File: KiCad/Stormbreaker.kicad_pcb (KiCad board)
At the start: 4 copper layers, 50.2 x 21 mm, 45 parts, among them J1 Micro_SD_Card_Det2, J2 USB_C_Receptacle_USB2.0_14P, J3 Conn_01x03, J4 FAN, Q1 PMOS, Q2 NMOS, SW1 SW_Push, U1 BQ25895RTW, U3 ATtiny1616-M

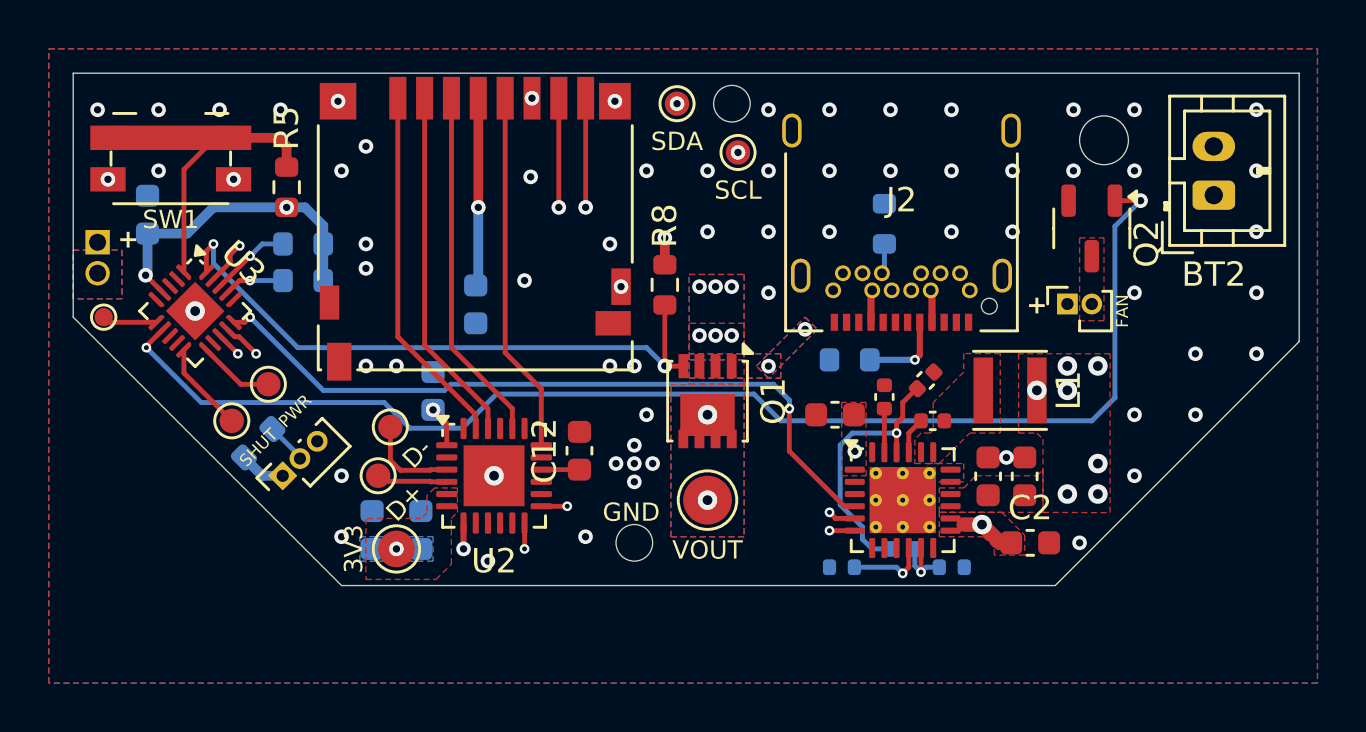
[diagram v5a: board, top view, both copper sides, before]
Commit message: Power and ground zones, gnd stitching
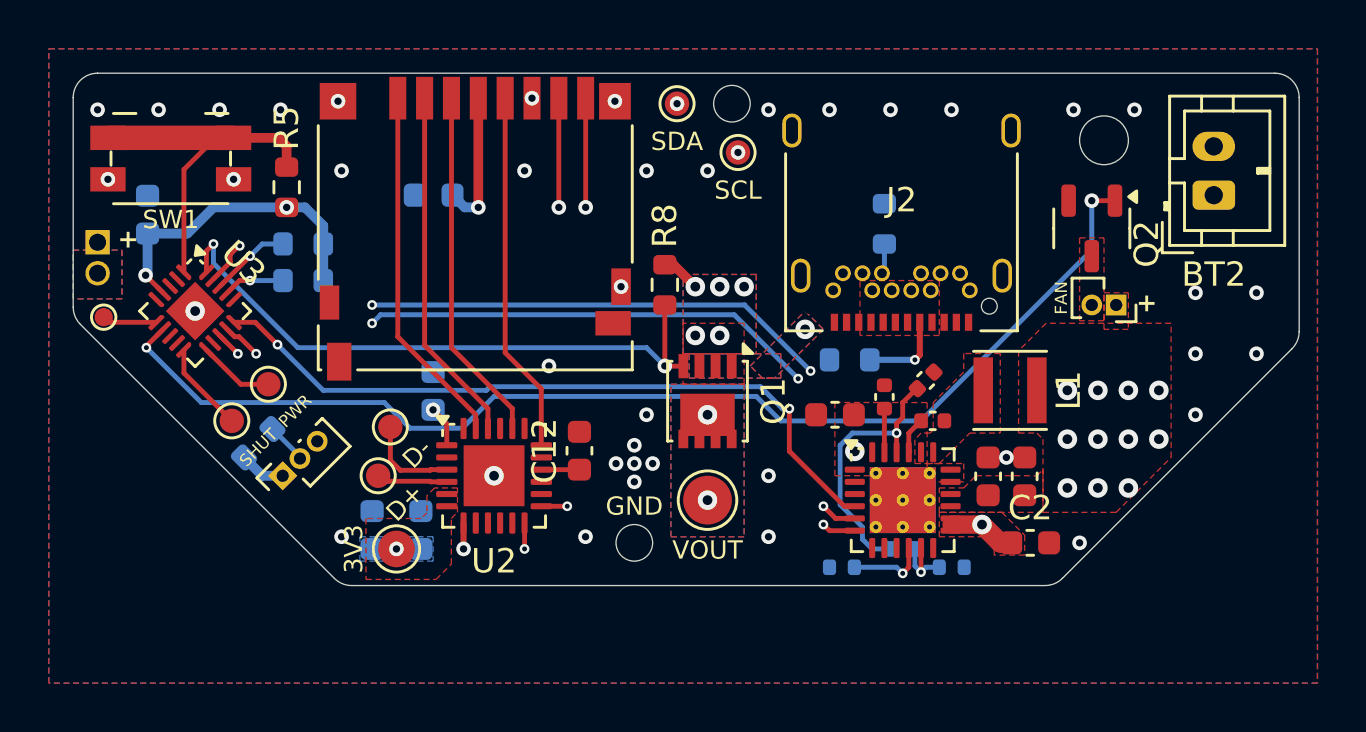
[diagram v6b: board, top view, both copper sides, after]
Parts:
- C7: value 60uF -> 22uF
- moved C11 4.80 mm to (128.8, 46.0), turned to 180 degrees
- moved J4 2.00 mm to (156.8, 50.5), turned to -90 degrees
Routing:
- net /BATT: track 63.5 -> 2.76 mm
- net VBUS: track 13.0 -> 0.14 mm
- net Net-(Q2-G): track 53.1 -> 48.0 mm
- net SD_VCC: track 24.8 -> 22.8 mm
- net VCC: track 16.0 -> 16.6 mm, vias 18 -> 19
- net SDA_2: track 34.6 -> 34.7 mm, vias 2 -> 4
- net SCL_2: track 35.6 -> 35.5 mm, vias 2 -> 4
- net GND: vias 67 -> 40
- added copper zone on In2.Cu, net /BATT
- added copper zone on In2.Cu, net VBUS
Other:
- outline, holes or cut-outs redrawn

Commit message: Nearing completion...but no idea how to mount it
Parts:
- removed TP8: SDA, TestPoint:TestPoint_Pad_D1.0mm
- removed TP9: SCL, TestPoint:TestPoint_Pad_D1.0mm
- added J5: Conn_01x02, Connector_PinSocket_1.00mm:PinSocket_1x02_P1.00mm_Vertical, F.Cu at (124.2, 59.4)
- C2: moved to B.Cu
- J2: footprint Connector_USB:USB_C_Receptacle_Amphenol_12401548E4-2A -> Connector_USB:USB_C_Receptacle_GCT_USB4105-xx-A_16P_TopMnt_Horizontal
- moved R4 9.12 mm to (149.2, 44.3), turned to -90 degrees
- moved C2 3.41 mm to (151.2, 57.5), turned to 90 degrees
- moved R6 3.02 mm to (146.2, 44.3)
- moved C8 2.16 mm to (127.0, 55.2), turned to 180 degrees
- moved J2 1.88 mm to (148.0, 44.3)
- moved SW1 1.00 mm to (118.0, 43.5)
- moved R2 0.78 mm to (149.8, 60.5), turned to -90 degrees
- moved C13 0.68 mm to (117.0, 47.5)
- moved L1 0.46 mm to (152.0, 53.8), turned to 90 degrees
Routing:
- net SCL: track 25.9 -> 9.73 mm, vias 2 -> 1
- net SDA: track 24.3 -> 10.6 mm, vias 2 -> 1
- net GND: track 0.00 -> 12.1 mm, vias 40 -> 32
- net VCC: track 16.6 -> 21.4 mm, vias 19 -> 34
- net /PA0: track 13.9 -> 10.2 mm
- net Net-(Q2-G): track 48.0 -> 51.5 mm
- net Net-(J4-Pin_2): track 0.00 -> 2.00 mm
- net Net-(Q1-G): track 25.6 -> 27.5 mm
- net Net-(J2-CC2): track 1.24 -> 2.84 mm, vias 0 -> 1
- net /BATT: track 2.76 -> 1.25 mm, vias 1 -> 9
- net Net-(U1-REGN): track 11.0 -> 12.3 mm
- net Net-(U2-VDD): track 1.68 -> 2.66 mm
- net Net-(U1-TS): track 2.87 -> 3.68 mm
- net SDA_2: track 34.7 -> 35.5 mm, vias 4 -> 3
- net /PowerButton: track 15.1 -> 15.7 mm
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- added copper zone on B.Cu, net VBUS
- removed copper zone on F.Cu, net Net-(J4-Pin_2)
- removed copper zone on In1.Cu, net VCC
- removed copper zone on In1.Cu, net VDD
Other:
- outline, holes or cut-outs redrawn
- board text added: "LED"

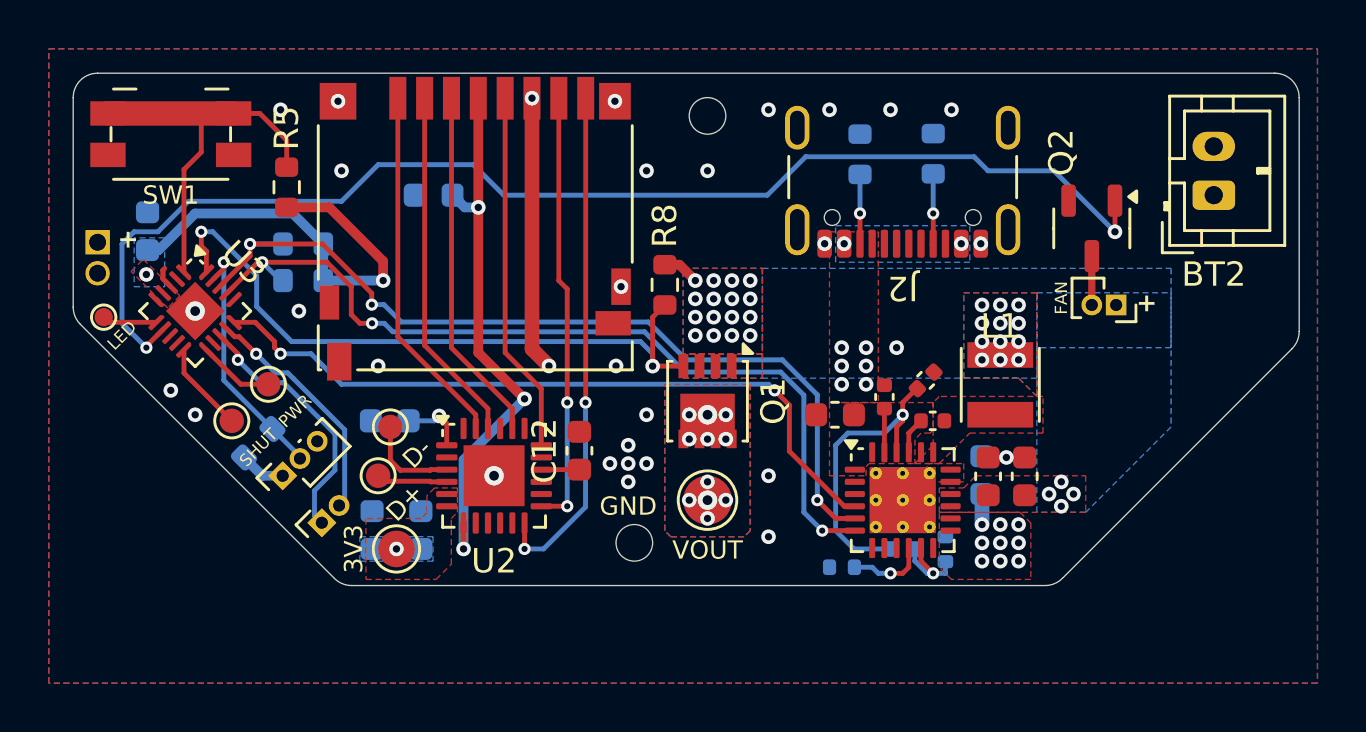
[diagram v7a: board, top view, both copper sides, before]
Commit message: Firmware development, minor hardware changes
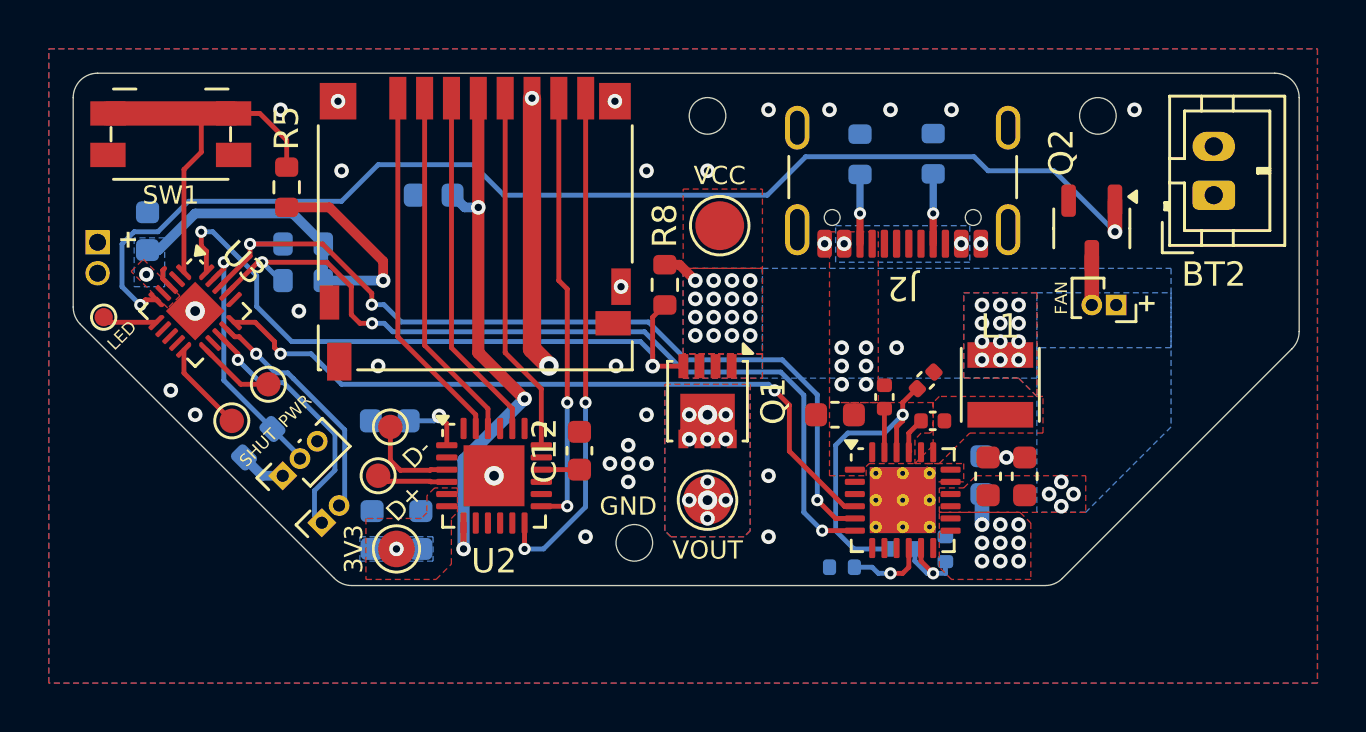
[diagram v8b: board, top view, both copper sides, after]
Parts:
- added TP8: VCC, TestPoint:TestPoint_Pad_D2.0mm, F.Cu at (140.5, 47.2)
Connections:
- U3 pad 5: unconnected-(U3-PA4-Pad5) -> Net-(Q2-G)
- U3 pad 7: Net-(Q2-G) -> unconnected-(U3-PA6-Pad7)
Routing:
- net Net-(Q2-G): track 51.5 -> 49.3 mm
- net GND: vias 32 -> 34
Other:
- outline, holes or cut-outs redrawn
